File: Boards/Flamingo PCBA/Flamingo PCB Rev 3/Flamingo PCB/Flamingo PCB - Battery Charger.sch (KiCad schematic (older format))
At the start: 10 parts

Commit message: Advanced schematic for battery charger
To do:

* Find a better connector for the switch than a JST PH2
* Check the polarity of the battery connector w.r.t. Adafruit batteries.
*Assign footprints
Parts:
- removed C? (x2): 10uF, symbol Device:CP1_Small
- removed J?: JST Battery conn, symbol MyConnectors:01x02_Connector
- removed J?: Wire Switch Here, symbol MyConnectors:01x02_Connector
- removed R? (x2): 2.0k, symbol MyResistors:R_vert
- added C301, C302: 10uF, Capacitors_SMD:C_0805_HandSoldering, symbol MyCapacitors:CP1_Small_vert
- added J301: Wire Switch Here, digikey-footprints:PinHeader_1x2_P2mm_Drill1mm_RA, symbol dk_Rectangular-Connectors-Headers-Male-Pins:S2B-PH-K-S_LF__SN_
- added J302: JST PH Battery Connector, digikey-footprints:PinHeader_1x2_P2mm_Drill1mm_RA, symbol dk_Rectangular-Connectors-Headers-Male-Pins:S2B-PH-K-S_LF__SN_
- added JP301: Solder Jumper, symbol Jumper:SolderJumper_2_Open
- added R302: 1.5k, Resistors_SMD:R_0603_HandSoldering, symbol MyResistors:R_vert
- added R303: 2.49k, Resistors_SMD:R_0603_HandSoldering, symbol MyResistors:R_vert
- added R304: 10k, Resistors_SMD:R_0603_HandSoldering, symbol MyResistors:R_vert
- D301: renamed from D?; footprint (none) -> LEDs:LED_0603_HandSoldering; Description (none) -> LED RED DIFFUSED 0603 SMD; Digi-Key_PN (none) -> 475-2506-1-ND; MFR P/N MFR P/N -> LS L29K-G1J2-1-Z; Manufacturer (none) -> OSRAM Opto Semiconductors Inc.; Package Size XXXX -> 0603; Website (none) -> https://www.digikey.com/en/products/detail/osram-opto-semic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
- D302: renamed from D?; Description (none) -> LED GREEN DIFFUSED 0603 SMD; Digi-Key_PN (none) -> 475-3118-1-ND; MFR P/N MFR P/N -> LG L29K-F2J1-24-Z; Manufacturer (none) -> OSRAM Opto Semiconductors Inc.; Package Size XXXX -> 0603; Website (none) -> https://www.digikey.com/en/products/detail/osram-opto-semic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
- R301: renamed from R?; value 2.0k -> 1.5k; footprint (none) -> Resistors_SMD:R_0603_HandSoldering; Description (none) -> RES SMD 1.5K OHM 1% 1/10W 0603; Digi-Key_PN (none) -> 311-1.50KHRCT-ND; MFR P/N MFR P/N -> RC0603FR-071K5L; Manufacturer (none) -> Yageo; Website (none) -> https://www.digikey.com/en/products/detail/yageo/RC0603FR-0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
- gave numbers to parts that had none: 1
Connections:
- wire segments 25 -> 34
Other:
- note added: "A search for 0603 OSRAM leds\n\nhttps://www.digikey.com/short/zwdccj\nBlue\nGreen\norange\nRed\nWhite\nWhite Cool\nYellow"
- note added: "CHECK POLARITY"
- note added: "HIGH when charging is done"
- note added: "NEED TO FIND A GOOD SOCKET FOR THE SWITCH CABLE\nMIGHT JUST NOT POPULATE AND SOLDER DIRECT"
- note added: "Open: 10k = 100 mA\nClosed: 2.0k = 500 mA\n\nBatt charging rate:\n\n10k = 100mA *\n5.0k = 200 mA\n2.0k = 500 mA *\n1.0k = 1000mA \n\nAdafruit typically does 0.5C for their batteries\n2500 mAh capacity - 1200 mA charge current"
- note added: "Vf = 1.8V, 2 mA Ityp\n5V-1.8 = 3.2V\n3.2V/1.5k = 2.1 mA"
- note removed: "Batt charging rate:\n10k = 100mA\n5.0k = 200 mA\n2.0k = 500 mA\n1.0k = 1000mA"
- note removed: "TODO\nChange resistor values\nFind green resistor"
- moved on the sheet: D301, D302, R301, U301

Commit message: Fixed footprint libraries to v5, added some footprints
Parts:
- D302: footprint (none) -> LEDs:LED_0603_HandSoldering
- JP301: footprint (none) -> Jumper:SolderJumper-2_P1.3mm_Open_Pad1.0x1.5mm
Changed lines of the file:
@@
 F 0 "D302" H 3767 4180 50  0000 L CNN
 F 1 "Green/Done" H 3767 4089 50  0000 L CNN
-F 2 "" H 3750 4050 50  0001 C CNN
+F 2 "LEDs:LED_0603_HandSoldering" H 3750 4050 50  0001 C CNN
 F 3 "https://dammedia.osram.info/media/resource/hires/osram-dam-2493945/LG%20L29K.pdf" H 3850 4150 50  0001 C CNN
 F 4 "0603" H 3767 3998 50  0000 L CNN "Package Size"
@@
 F 0 "JP301" V 5804 3318 50  0000 L CNN
 F 1 "Solder Jumper" V 5895 3318 50  0000 L CNN
-F 2 "" H 5850 3250 50  0001 C CNN
+F 2 "Jumper:SolderJumper-2_P1.3mm_Open_Pad1.0x1.5mm" H 5850 3250 50  0001 C CNN
 F 3 "~" H 5850 3250 50  0001 C CNN
 	1    5850 3250

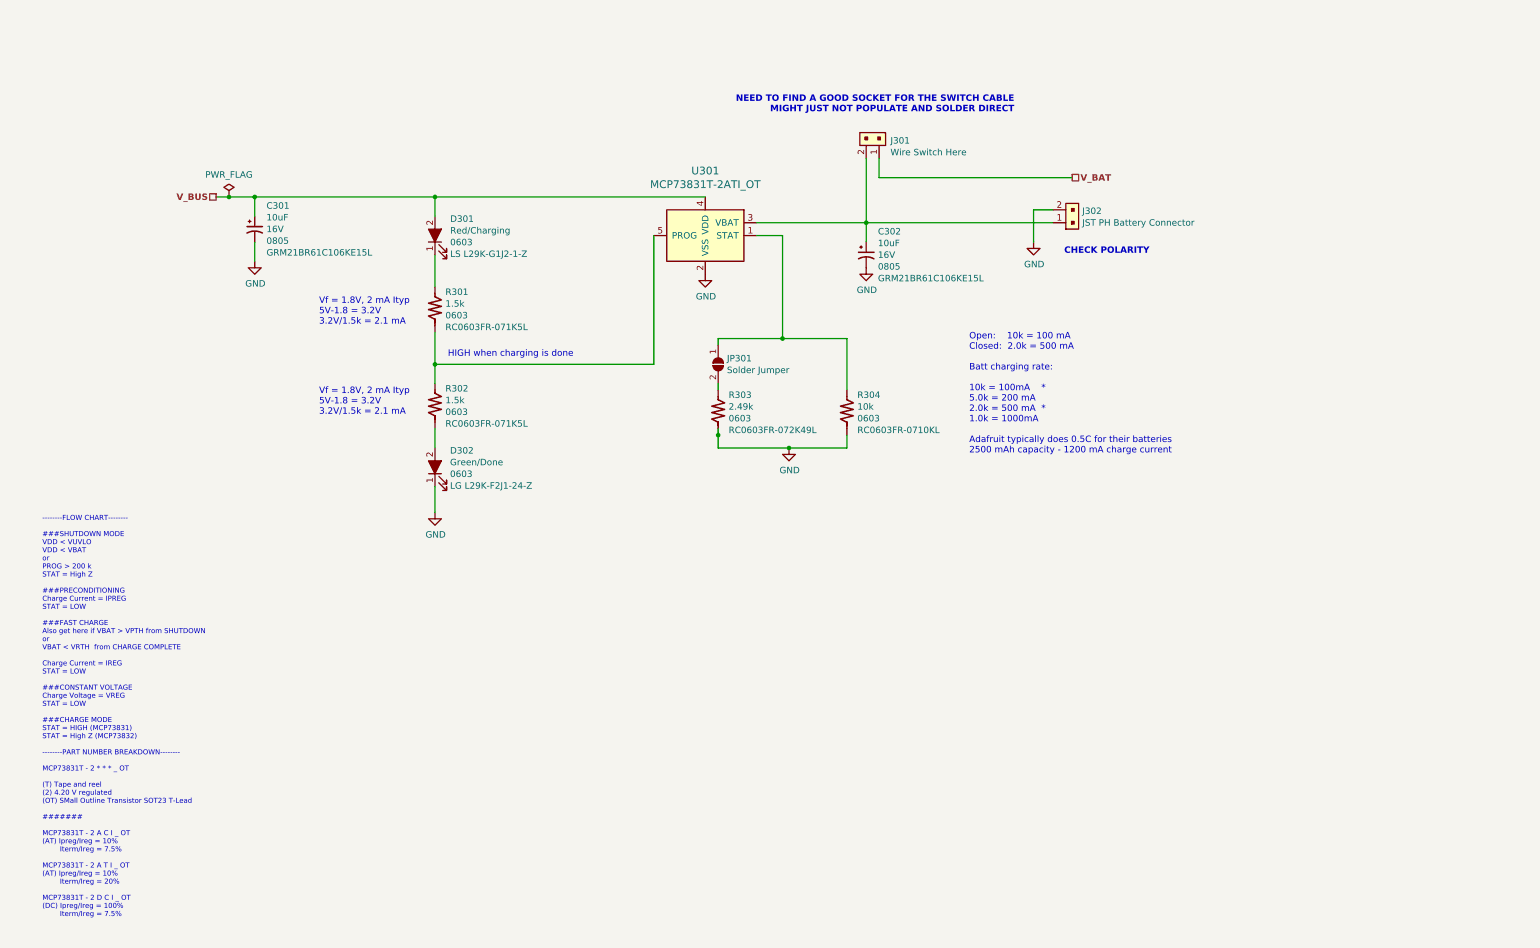
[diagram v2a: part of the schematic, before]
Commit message: Changed ATMEGA328P for a modified DK symbol
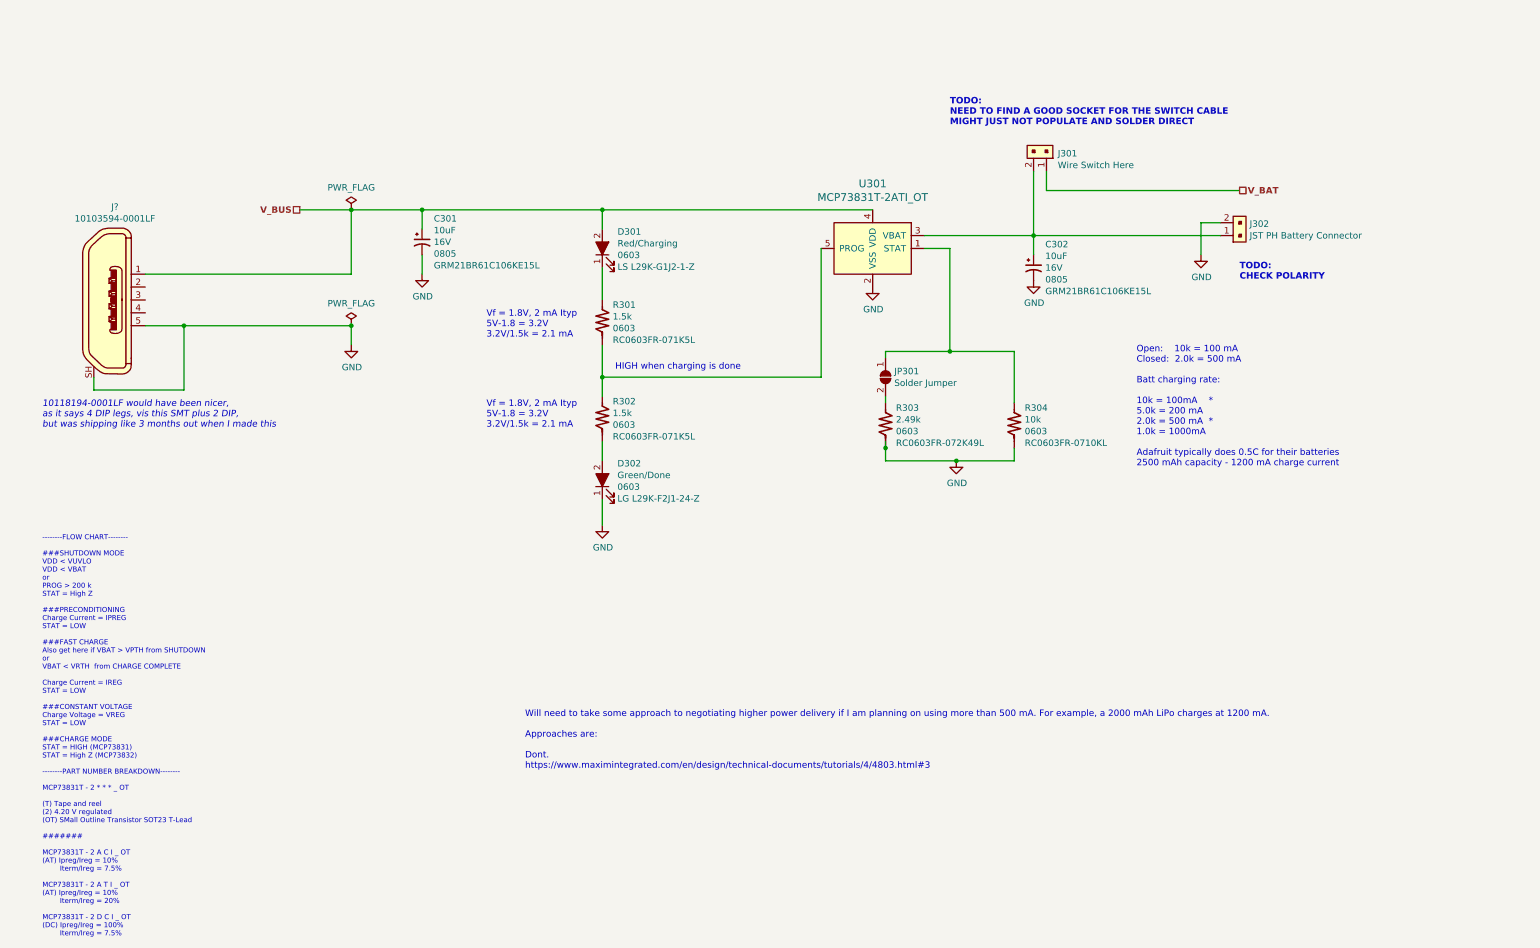
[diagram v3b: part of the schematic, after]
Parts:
- added J?: 10103594-0001LF, digikey-footprints:USB_Micro_B_Female_10103594-0001LF, symbol dk_USB-DVI-HDMI-Connectors:10103594-0001LF
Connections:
- wire segments 34 -> 42
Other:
- note added: "10118194-0001LF would have been nicer, \nas it says 4 DIP legs, vis this SMT plus 2 DIP,\nbut was shipping like 3 months out when I made this"
- note added: "TODO:\nCHECK POLARITY"
- note added: "TODO:\nNEED TO FIND A GOOD SOCKET FOR THE SWITCH CABLE\nMIGHT JUST NOT POPULATE AND SOLDER DIRECT"
- note added: "Will need to take some approach to negotiating higher power delivery if I am planning on using more than 500 mA. For example, a 2000 mAh LiPo charges at 1200 mA.\n\nApproaches are:\n\nDont.\nhttps://www.maximintegrated.com/en/design/technical-documents/tutorials/4/4803.html#3"
- note removed: "CHECK POLARITY"
- note removed: "NEED TO FIND A GOOD SOCKET FOR THE SWITCH CABLE\nMIGHT JUST NOT POPULATE AND SOLDER DIRECT"
- moved on the sheet: C301, C302, D301, D302, J301, J302, JP301, R301, R302, R303, R304, U301

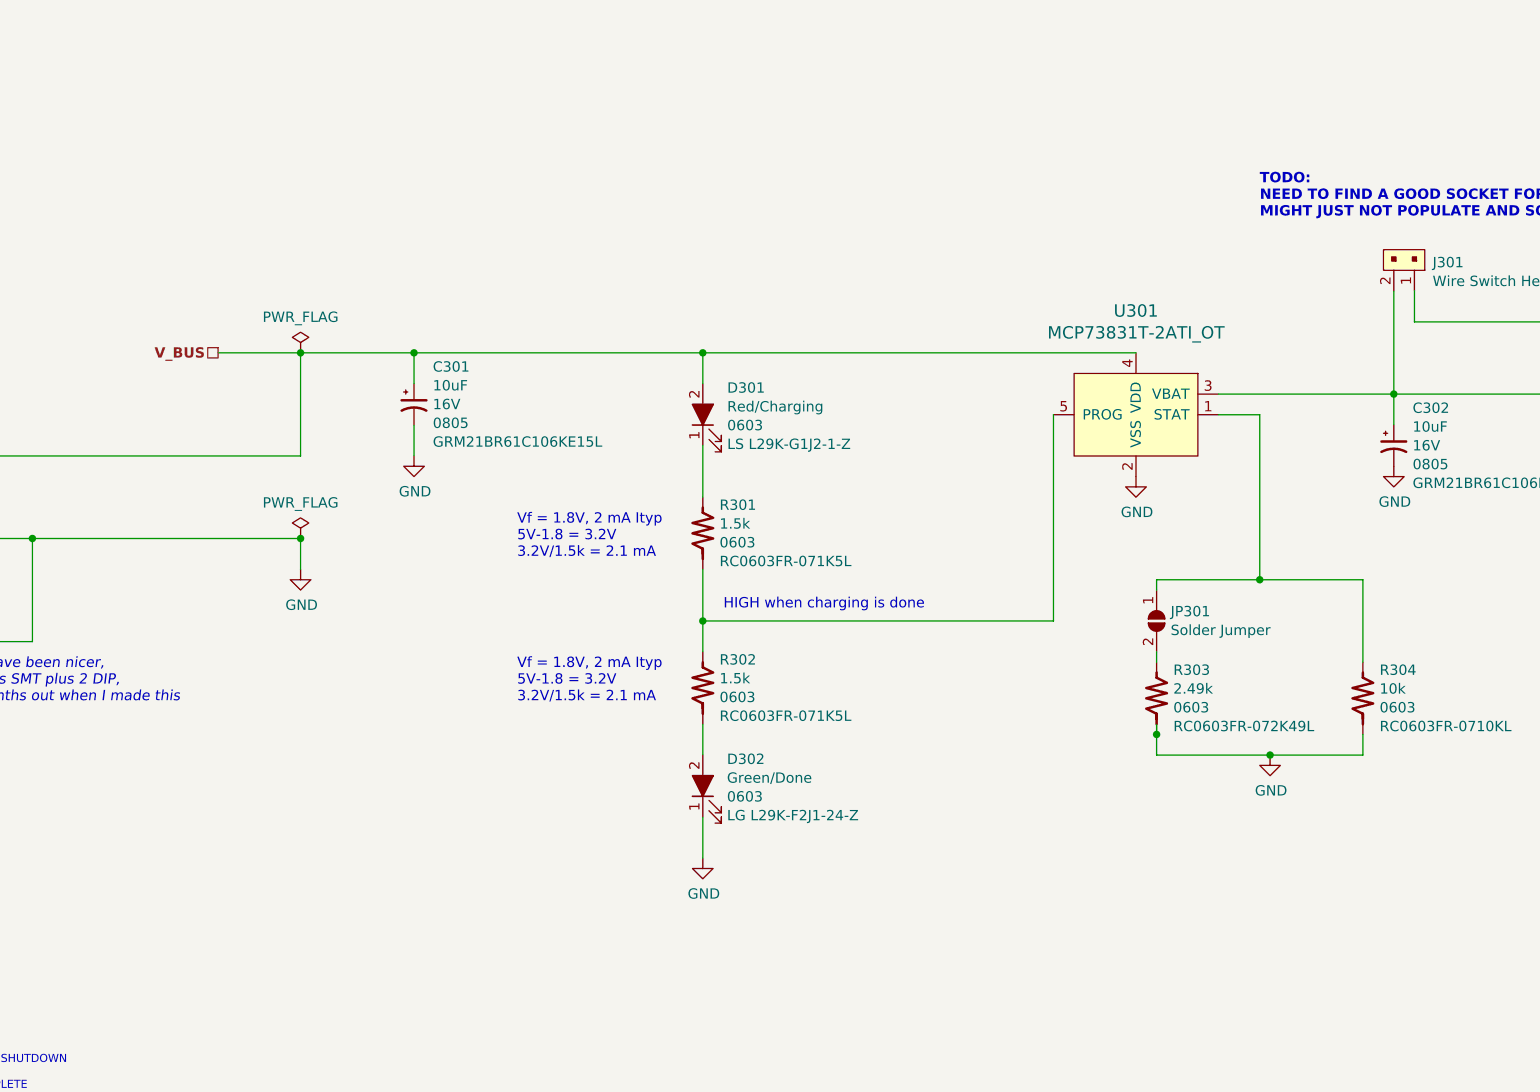
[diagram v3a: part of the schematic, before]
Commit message: Worked on Power board mainly.
Still have to resolve the power sharing.
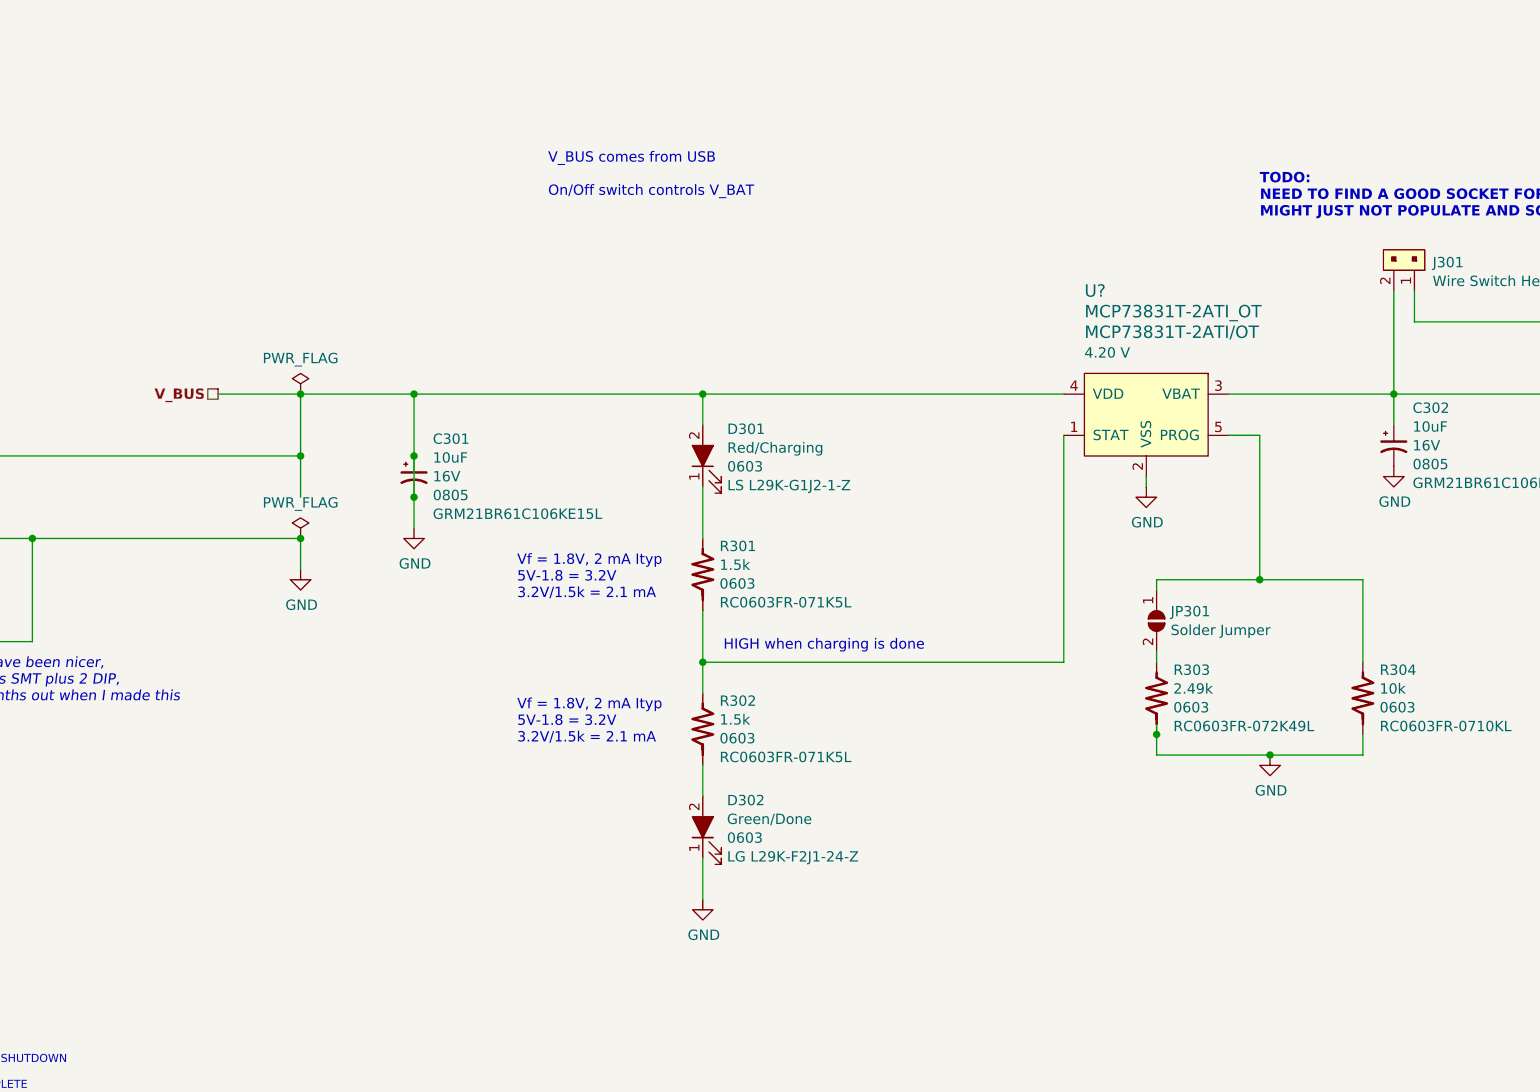
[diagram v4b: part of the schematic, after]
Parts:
- removed U301: MCP73831T-2ATI_OT, digikey-footprints:SOT-753, symbol dk_PMIC-Battery-Chargers:MCP73831T-2ATI_OT
- added U?: MCP73831T-2ATI_OT, digikey-footprints:SOT-753, symbol MyICs:MCP73831T-2ATI_OT
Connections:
- wire segments 42 -> 45
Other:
- note added: "V_BUS comes from USB\n\nOn/Off switch controls V_BAT"
- moved on the sheet: C301, D301, D302, R301, R302
